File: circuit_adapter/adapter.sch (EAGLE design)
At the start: 10 parts, among them CN1 5035521020, X1 2510-

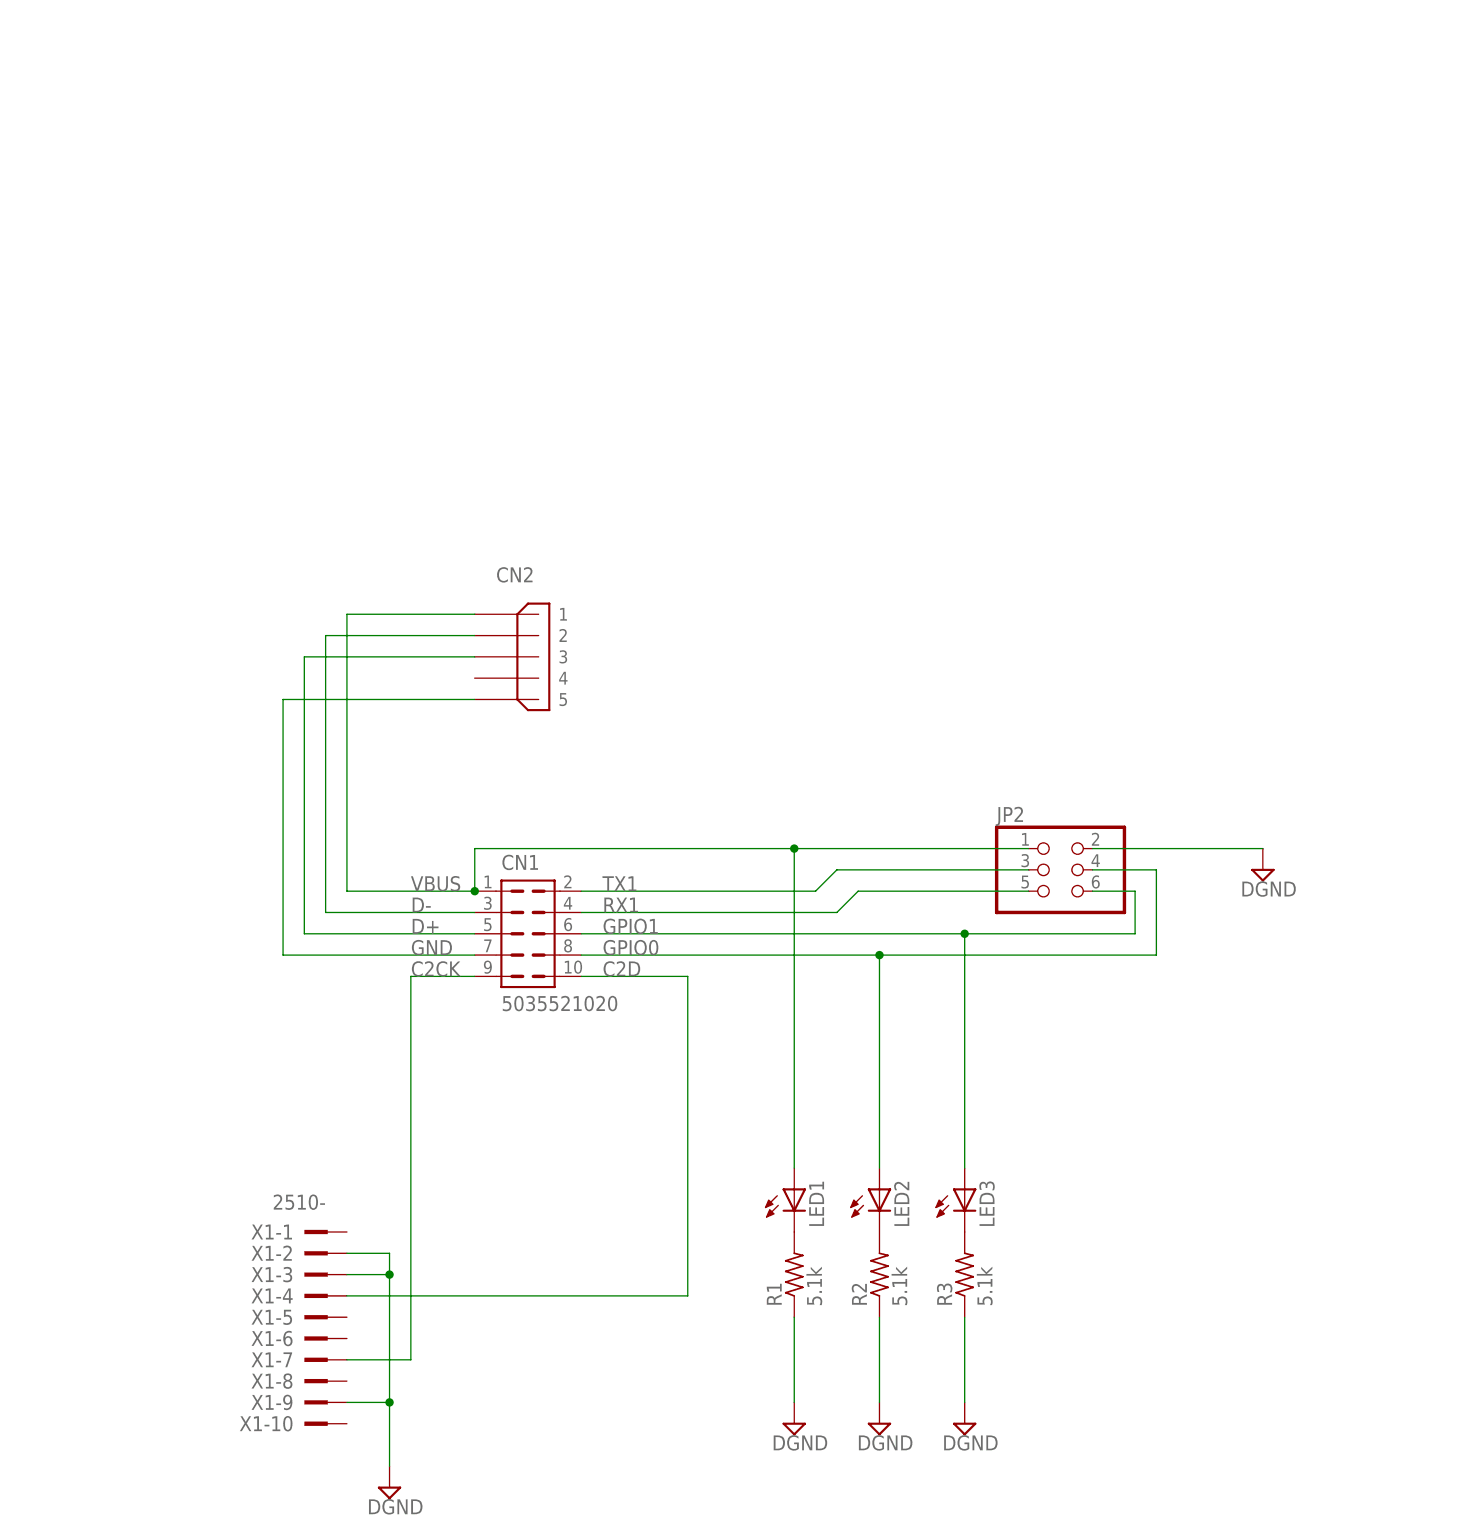
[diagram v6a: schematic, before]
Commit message: Modified adapter circuit
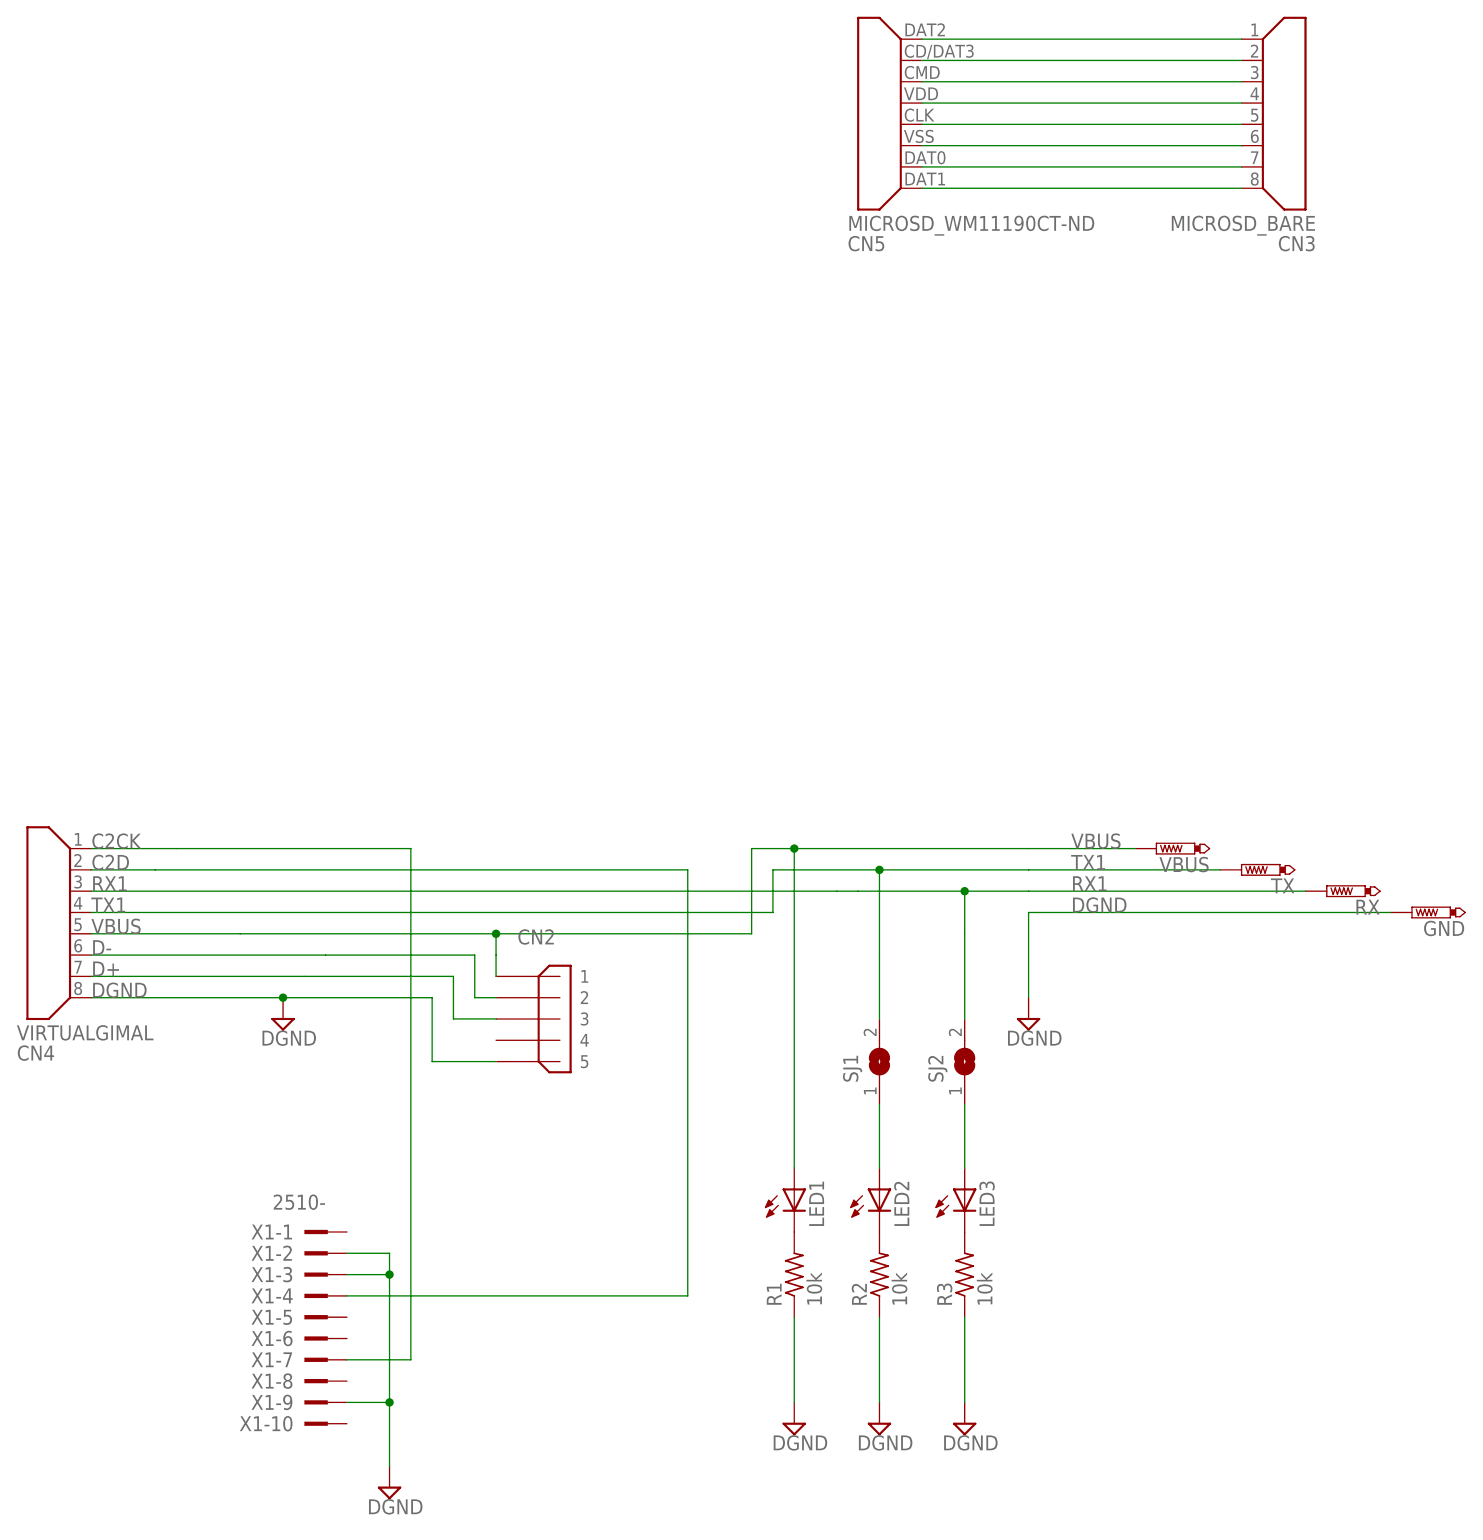
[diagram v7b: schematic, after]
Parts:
- removed CN1: 5035521020, connector:5035521020
- removed JP2: (no value), pinhead:PINHD-2X3
- added CN3: MICROSD_BARE, connector:MICROSD_BARE
- added CN4: VIRTUALGIMAL, connector:VIRTUALGIMAL
- added CN5: MICROSD_WM11190CT-ND, connector:MICROSD_WM11190CT-ND
- added GND, RX, TX, VBUS: PTR1TP19R, testpad:PTR1TP19R
- added SJ1, SJ2: (no value), jumper:SJ
- R1, R2, R3: value 5.1k -> 10k
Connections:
- removed net GND: CN1.7, CN2.5, JP2.2, R1.1, R2.1, R3.1, X1-2.KL, X1-3.KL, X1-9.KL
- removed net GPIO0: CN1.8, JP2.4, LED2.A
- removed net GPIO1: CN1.6, JP2.6, LED3.A
- new net DGND: CN2.5, CN4.P$8, GND.TP, R1.1, R2.1, R3.1, X1-2.KL, X1-3.KL, X1-9.KL
- new net N$10: CN3.P$7, CN5.P$7
- new net N$11: CN3.P$8, CN5.P$8
- new net N$12: LED2.A, SJ1.1
- new net N$13: LED3.A, SJ2.1
- new net N$4: CN3.P$1, CN5.P$1
- new net N$5: CN3.P$2, CN5.P$2
- new net N$6: CN3.P$3, CN5.P$3
- new net N$7: CN3.P$4, CN5.P$4
- new net N$8: CN3.P$5, CN5.P$5
- new net N$9: CN3.P$6, CN5.P$6
- net C2CK: now also CN4.P$1; no longer CN1.9
- net C2D: now also CN4.P$2; no longer CN1.10
- net D+: now also CN4.P$7; no longer CN1.5
- net D-: now also CN4.P$6; no longer CN1.3
- net RX1: now also CN4.P$3, RX.TP, SJ2.2; no longer CN1.4, JP2.5
- net TX1: now also CN4.P$4, SJ1.2, TX.TP; no longer CN1.2, JP2.3
- net VBUS: now also CN4.P$5, VBUS.TP; no longer CN1.1, JP2.1
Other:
- moved on the sheet: CN2

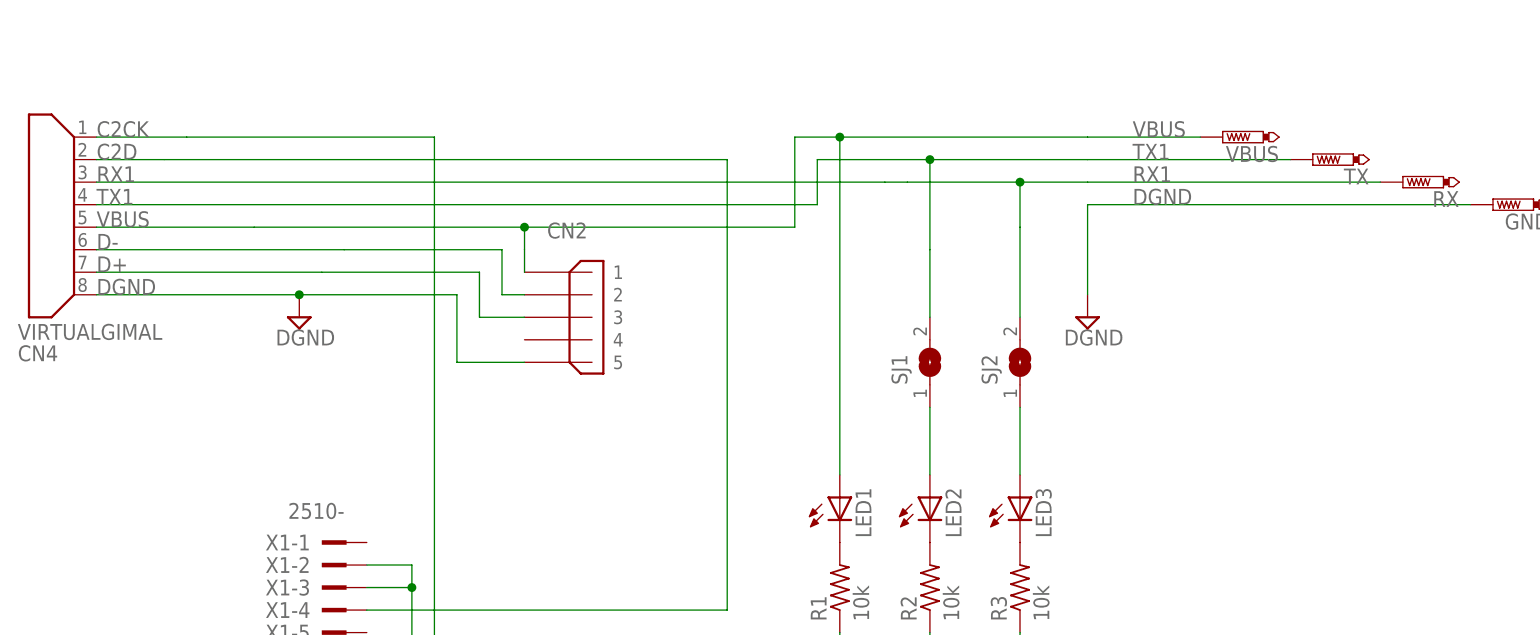
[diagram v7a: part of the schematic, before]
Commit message: Modified circuit adapter
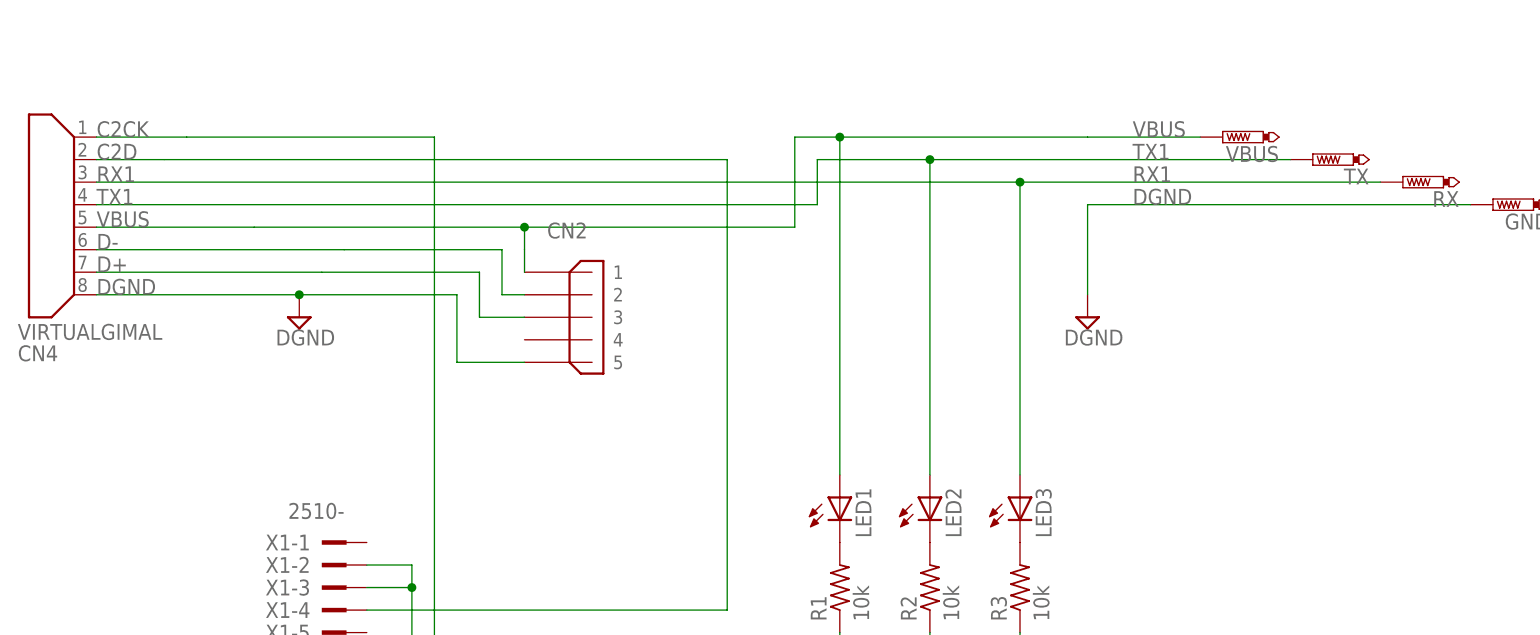
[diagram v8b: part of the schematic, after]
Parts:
- removed SJ1, SJ2: (no value), jumper:SJ
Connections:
- removed net N$12: LED2.A, SJ1.1
- removed net N$13: LED3.A, SJ2.1
- net RX1: now also LED3.A; no longer SJ2.2
- net TX1: now also LED2.A; no longer SJ1.2
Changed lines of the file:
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@@
 <part name="RX" library="testpad" library_urn="urn:adsk.eagle:library:385" deviceset="PTR1" device="TP19R" package3d_urn="urn:adsk.eagle:package:27972/1"/>
 <part name="GND" library="testpad" library_urn="urn:adsk.eagle:library:385" deviceset="PTR1" device="TP19R" package3d_urn="urn:adsk.eagle:package:27972/1"/>
-<part name="SJ1" library="jumper" library_urn="urn:adsk.eagle:library:252" deviceset="SJ" device="" package3d_urn="urn:adsk.eagle:package:15471/1"/>
-<part name="SJ2" library="jumper" library_urn="urn:adsk.eagle:library:252" deviceset="SJ" device="" package3d_urn="urn:adsk.eagle:package:15471/1"/>
 </parts>
 <sheets>
@@
 <instance part="RX" gate="G$1" x="137.16" y="66.04" rot="R90"/>
 <instance part="GND" gate="G$1" x="147.32" y="63.5" rot="R90"/>
-<instance part="SJ1" gate="1" x="83.82" y="45.72" rot="R90"/>
-<instance part="SJ2" gate="1" x="93.98" y="45.72" rot="R90"/>
 </instances>
 <busses>
@@
 <label x="-10.16" y="63.5" size="1.778" layer="95"/>
 <pinref part="CN4" gate="G$1" pin="P$4"/>
-<wire x1="83.82" y1="68.58" x2="101.6" y2="68.58" width="0.1524" layer="91"/>
 <wire x1="-10.16" y1="63.5" x2="71.12" y2="63.5" width="0.1524" layer="91"/>
 <wire x1="71.12" y1="63.5" x2="71.12" y2="68.58" width="0.1524" layer="91"/>
-<wire x1="83.82" y1="50.8" x2="83.82" y2="58.42" width="0.1524" layer="91"/>
-<wire x1="83.82" y1="68.58" x2="83.82" y2="58.42" width="0.1524" layer="91"/>
 <junction x="83.82" y="68.58"/>
 <pinref part="TX" gate="G$1" pin="TP"/>
-<wire x1="124.46" y1="68.58" x2="101.6" y2="68.58" width="0.1524" layer="91"/>
+<wire x1="124.46" y1="68.58" x2="83.82" y2="68.58" width="0.1524" layer="91"/>
 <label x="106.68" y="68.58" size="1.778" layer="95"/>
-<pinref part="SJ1" gate="1" pin="2"/>
+<pinref part="LED2" gate="G$1" pin="A"/>
+<wire x1="83.82" y1="33.02" x2="83.82" y2="68.58" width="0.1524" layer="91"/>
 </segment>
 </net>
@@
 <net name="RX1" class="1">
 <segment>
-<wire x1="93.98" y1="50.8" x2="93.98" y2="60.96" width="0.1524" layer="91"/>
-<wire x1="101.6" y1="66.04" x2="93.98" y2="66.04" width="0.1524" layer="91"/>
-<wire x1="93.98" y1="66.04" x2="81.28" y2="66.04" width="0.1524" layer="91"/>
 <label x="-10.16" y="66.04" size="1.778" layer="95"/>
-<wire x1="81.28" y1="66.04" x2="78.74" y2="66.04" width="0.1524" layer="91"/>
 <pinref part="CN4" gate="G$1" pin="P$3"/>
-<wire x1="78.74" y1="66.04" x2="-10.16" y2="66.04" width="0.1524" layer="91"/>
-<wire x1="93.98" y1="60.96" x2="93.98" y2="66.04" width="0.1524" layer="91"/>
+<wire x1="93.98" y1="66.04" x2="-10.16" y2="66.04" width="0.1524" layer="91"/>
 <junction x="93.98" y="66.04"/>
 <pinref part="RX" gate="G$1" pin="TP"/>
-<wire x1="101.6" y1="66.04" x2="134.62" y2="66.04" width="0.1524" layer="91"/>
+<wire x1="93.98" y1="66.04" x2="134.62" y2="66.04" width="0.1524" layer="91"/>
 <label x="106.68" y="66.04" size="1.778" layer="95"/>
-<pinref part="SJ2" gate="1" pin="2"/>
-</segment>
-</net>
-<net name="N$12" class="1">
-<segment>
-<pinref part="SJ1" gate="1" pin="1"/>
-<pinref part="LED2" gate="G$1" pin="A"/>
-<wire x1="83.82" y1="33.02" x2="83.82" y2="40.64" width="0.1524" layer="91"/>
-</segment>
-</net>
-<net name="N$13" class="1">
-<segment>
-<pinref part="SJ2" gate="1" pin="1"/>
 <pinref part="LED3" gate="G$1" pin="A"/>
-<wire x1="93.98" y1="33.02" x2="93.98" y2="40.64" width="0.1524" layer="91"/>
-</segment>
-</net>
+<wire x1="93.98" y1="66.04" x2="93.98" y2="33.02" width="0.1524" layer="91"/>
+</segment>
+</net>
